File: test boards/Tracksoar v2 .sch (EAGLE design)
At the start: 45 parts, among them IC1 BME280, IC2 74AHC1G125DBV, Y1 16MHZ

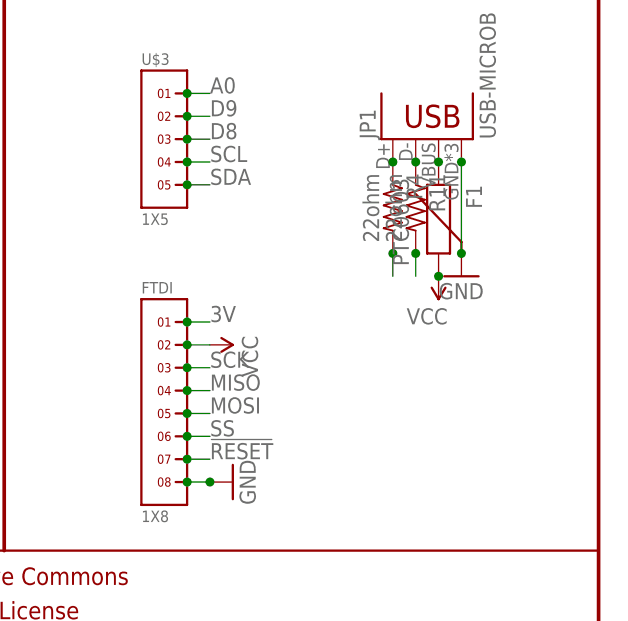
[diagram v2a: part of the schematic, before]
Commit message: Corrected battery connector placement
Moved the battery connector to the bottom side of the board to avoid
conflicts with the USB connector
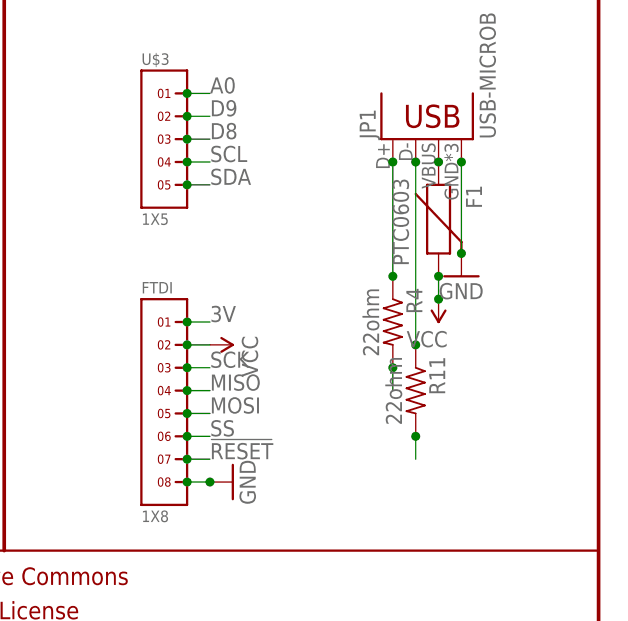
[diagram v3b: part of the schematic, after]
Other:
- moved on the sheet: R11, R4
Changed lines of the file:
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@@
 <instance part="JP1" gate="G$1" x="233.68" y="81.28" rot="R90"/>
 <instance part="J1" gate="G$1" x="38.1" y="177.8" rot="R270"/>
-<instance part="R4" gate="G$1" x="226.06" y="73.66" rot="R270"/>
-<instance part="R11" gate="G$1" x="228.6" y="73.66" rot="R270"/>
+<instance part="R4" gate="G$1" x="226.06" y="60.96" rot="R270"/>
+<instance part="R11" gate="G$1" x="228.6" y="53.34" rot="R270"/>
 <instance part="GND32" gate="1" x="233.68" y="66.04"/>
 <instance part="F1" gate="G$1" x="231.14" y="73.66" rot="R270"/>
-<instance part="SUPPLY15" gate="G$1" x="231.14" y="66.04" rot="R180"/>
+<instance part="SUPPLY15" gate="G$1" x="231.14" y="63.5" rot="R180"/>
 <instance part="SUPPLY16" gate="G$1" x="22.86" y="63.5" rot="R90"/>
 <instance part="C5" gate="G$1" x="12.7" y="58.42" rot="R90"/>
@@
 <pinref part="F1" gate="G$1" pin="2"/>
 <pinref part="SUPPLY15" gate="G$1" pin="VCC"/>
+<wire x1="231.14" y1="63.5" x2="231.14" y2="66.04" width="0.1524" layer="91"/>
 <junction x="231.14" y="66.04"/>
+<junction x="231.14" y="63.5"/>
 </segment>
 <segment>
@@
 <pinref part="JP1" gate="G$1" pin="D-"/>
 <pinref part="R11" gate="G$1" pin="1"/>
+<wire x1="228.6" y1="58.42" x2="228.6" y2="78.74" width="0.1524" layer="91"/>
+<junction x="228.6" y="58.42"/>
 <junction x="228.6" y="78.74"/>
 </segment>
@@
 <pinref part="JP1" gate="G$1" pin="D+"/>
 <pinref part="R4" gate="G$1" pin="1"/>
+<wire x1="226.06" y1="66.04" x2="226.06" y2="78.74" width="0.1524" layer="91"/>
+<junction x="226.06" y="66.04"/>
 <junction x="226.06" y="78.74"/>
 </segment>
@@
 <segment>
 <pinref part="R4" gate="G$1" pin="2"/>
-<wire x1="226.06" y1="68.58" x2="226.06" y2="66.04" width="0.1524" layer="91"/>
-<junction x="226.06" y="68.58"/>
+<wire x1="226.06" y1="55.88" x2="226.06" y2="53.34" width="0.1524" layer="91"/>
+<junction x="226.06" y="55.88"/>
 </segment>
 <segment>
@@
 <segment>
 <pinref part="R11" gate="G$1" pin="2"/>
-<wire x1="228.6" y1="68.58" x2="228.6" y2="66.04" width="0.1524" layer="91"/>
-<junction x="228.6" y="68.58"/>
-</segment>
-<segment>
+<wire x1="228.6" y1="48.26" x2="228.6" y2="45.72" width="0.1524" layer="91"/>
+<junction x="228.6" y="48.26"/>
+</segment>
+<segment>

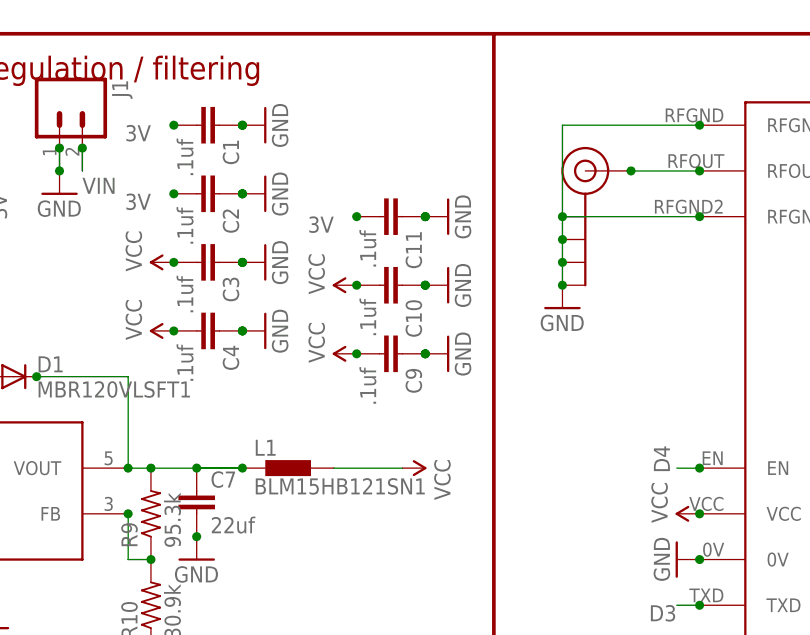
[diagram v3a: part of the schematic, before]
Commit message: Tracksoar V1.3
Created a new test board Tracksoar v1.3 to resolve potential issues
with the boost converter interfering with GPS reception.
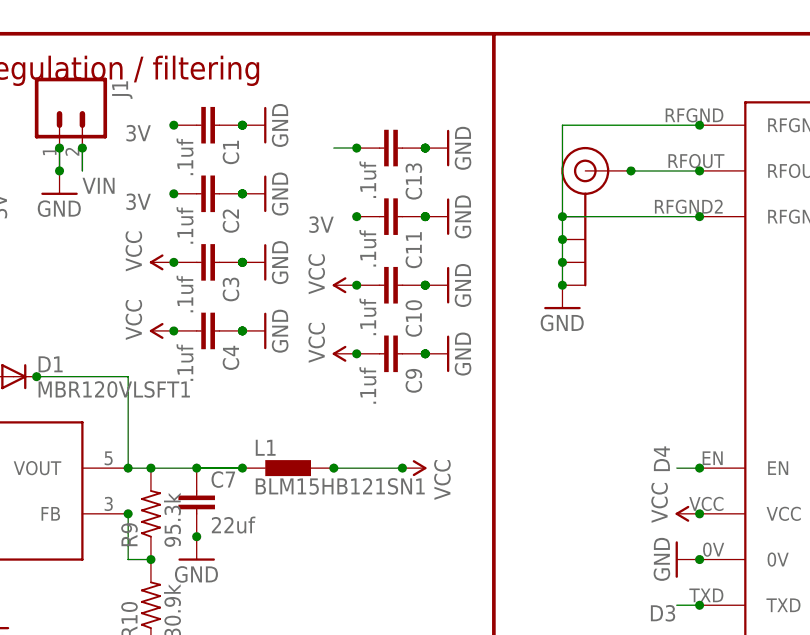
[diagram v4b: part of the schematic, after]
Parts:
- added C13: .1uf, SparkFun-Capacitors:CAP0402-CAP
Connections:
- net GND: now also C13.1
- net VIN: now also C13.2
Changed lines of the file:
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@@
 <grid distance="0.1" unitdist="inch" unit="inch" style="lines" multiple="1" display="no" altdistance="0.01" altunitdist="inch" altunit="inch"/>
 <layers>
-<layer number="1" name="Top" color="4" fill="1" visible="yes" active="no"/>
-<layer number="2" name="Route2" color="1" fill="3" visible="yes" active="no"/>
-<layer number="3" name="Route3" color="4" fill="3" visible="yes" active="no"/>
-<layer number="14" name="Route14" color="1" fill="6" visible="yes" active="no"/>
-<layer number="15" name="Route15" color="4" fill="6" visible="yes" active="no"/>
-<layer number="16" name="Bottom" color="1" fill="1" visible="yes" active="no"/>
-<layer number="17" name="Pads" color="2" fill="1" visible="yes" active="no"/>
-<layer number="18" name="Vias" color="2" fill="1" visible="yes" active="no"/>
-<layer number="19" name="Unrouted" color="6" fill="1" visible="yes" active="no"/>
-<layer number="20" name="Dimension" color="15" fill="1" visible="yes" active="no"/>
-<layer number="21" name="tPlace" color="7" fill="1" visible="yes" active="no"/>
-<layer number="22" name="bPlace" color="7" fill="1" visible="yes" active="no"/>
-<layer number="23" name="tOrigins" color="15" fill="1" visible="yes" active="no"/>
-<layer number="24" name="bOrigins" color="15" fill="1" visible="yes" active="no"/>
-<layer number="25" name="tNames" color="7" fill="1" visible="yes" active="no"/>
-<layer number="26" name="bNames" color="7" fill="1" visible="yes" active="no"/>
-<layer number="27" name="tValues" color="7" fill="1" visible="yes" active="no"/>
-<layer number="28" name="bValues" color="7" fill="1" visible="yes" active="no"/>
+<layer number="1" name="Top" color="4" fill="1" visible="no" active="no"/>
+<layer number="2" name="Route2" color="1" fill="3" visible="no" active="no"/>
+<layer number="3" name="Route3" color="4" fill="3" visible="no" active="no"/>
+<layer number="14" name="Route14" color="1" fill="6" visible="no" active="no"/>
+<layer number="15" name="Route15" color="4" fill="6" visible="no" active="no"/>
+<layer number="16" name="Bottom" color="1" fill="1" visible="no" active="no"/>
+<layer number="17" name="Pads" color="2" fill="1" visible="no" active="no"/>
+<layer number="18" name="Vias" color="2" fill="1" visible="no" active="no"/>
+<layer number="19" name="Unrouted" color="6" fill="1" visible="no" active="no"/>
+<layer number="20" name="Dimension" color="15" fill="1" visible="no" active="no"/>
+<layer number="21" name="tPlace" color="7" fill="1" visible="no" active="no"/>
+<layer number="22" name="bPlace" color="7" fill="1" visible="no" active="no"/>
+<layer number="23" name="tOrigins" color="15" fill="1" visible="no" active="no"/>
+<layer number="24" name="bOrigins" color="15" fill="1" visible="no" active="no"/>
+<layer number="25" name="tNames" color="7" fill="1" visible="no" active="no"/>
+<layer number="26" name="bNames" color="7" fill="1" visible="no" active="no"/>
+<layer number="27" name="tValues" color="7" fill="1" visible="no" active="no"/>
+<layer number="28" name="bValues" color="7" fill="1" visible="no" active="no"/>
 <layer number="29" name="tStop" color="7" fill="3" visible="no" active="no"/>
 <layer number="30" name="bStop" color="7" fill="6" visible="no" active="no"/>
@@
 <layer number="35" name="tGlue" color="7" fill="4" visible="no" active="no"/>
 <layer number="36" name="bGlue" color="7" fill="5" visible="no" active="no"/>
-<layer number="37" name="tTest" color="7" fill="1" visible="yes" active="no"/>
-<layer number="38" name="bTest" color="7" fill="1" visible="yes" active="no"/>
+<layer number="37" name="tTest" color="7" fill="1" visible="no" active="no"/>
+<layer number="38" name="bTest" color="7" fill="1" visible="no" active="no"/>
 <layer number="39" name="tKeepout" color="4" fill="11" visible="no" active="no"/>
 <layer number="40" name="bKeepout" color="1" fill="11" visible="no" active="no"/>
@@
 <layer number="44" name="Drills" color="7" fill="1" visible="no" active="no"/>
 <layer number="45" name="Holes" color="7" fill="1" visible="no" active="no"/>
-<layer number="46" name="Milling" color="3" fill="1" visible="yes" active="no"/>
-<layer number="47" name="Measures" color="7" fill="1" visible="yes" active="no"/>
-<layer number="48" name="Document" color="7" fill="1" visible="yes" active="no"/>
-<layer number="49" name="Reference" color="7" fill="1" visible="yes" active="no"/>
-<layer number="50" name="dxf" color="7" fill="1" visible="yes" active="no"/>
-<layer number="51" name="tDocu" color="7" fill="1" visible="yes" active="no"/>
-<layer number="52" name="bDocu" color="7" fill="1" visible="yes" active="no"/>
-<layer number="53" name="tGND_GNDA" color="7" fill="9" visible="yes" active="no"/>
-<layer number="54" name="bGND_GNDA" color="1" fill="9" visible="yes" active="no"/>
-<layer number="56" name="wert" color="7" fill="1" visible="yes" active="no"/>
-<layer number="57" name="tCAD" color="7" fill="1" visible="yes" active="no"/>
-<layer number="59" name="tCarbon" color="7" fill="1" visible="yes" active="no"/>
-<layer number="60" name="bCarbon" color="7" fill="1" visible="yes" active="no"/>
+<layer number="46" name="Milling" color="3" fill="1" visible="no" active="no"/>
+<layer number="47" name="Measures" color="7" fill="1" visible="no" active="no"/>
+<layer number="48" name="Document" color="7" fill="1" visible="no" active="no"/>
+<layer number="49" name="Reference" color="7" fill="1" visible="no" active="no"/>
+<layer number="50" name="dxf" color="7" fill="1" visible="no" active="no"/>
+<layer number="51" name="tDocu" color="7" fill="1" visible="no" active="no"/>
+<layer number="52" name="bDocu" color="7" fill="1" visible="no" active="no"/>
+<layer number="53" name="tGND_GNDA" color="7" fill="9" visible="no" active="no"/>
+<layer number="54" name="bGND_GNDA" color="1" fill="9" visible="no" active="no"/>
+<layer number="56" name="wert" color="7" fill="1" visible="no" active="no"/>
+<layer number="57" name="tCAD" color="7" fill="1" visible="no" active="no"/>
+<layer number="59" name="tCarbon" color="7" fill="1" visible="no" active="no"/>
+<layer number="60" name="bCarbon" color="7" fill="1" visible="no" active="no"/>
 <layer number="90" name="Modules" color="5" fill="1" visible="yes" active="yes"/>
 <layer number="91" name="Nets" color="2" fill="1" visible="yes" active="yes"/>
@@
 <part name="GND16" library="SparkFun-Aesthetics" deviceset="GND" device=""/>
 <part name="C12" library="SparkFun-Capacitors" deviceset="CAP" device="0402-CAP" value="1uf"/>
+<part name="C13" library="SparkFun-Capacitors" deviceset="CAP" device="0402-CAP" value=".1uf"/>
+<part name="GND19" library="SparkFun-Aesthetics" deviceset="GND" device=""/>
 </parts>
 <sheets>
@@
 <instance part="GND16" gate="1" x="81.28" y="165.1" rot="R90"/>
 <instance part="C12" gate="G$1" x="17.78" y="73.66" rot="R90"/>
+<instance part="C13" gate="G$1" x="73.66" y="172.72" rot="R270"/>
+<instance part="GND19" gate="1" x="81.28" y="172.72" rot="R90"/>
 </instances>
 <busses>
@@
 <label x="7.62" y="73.66" size="1.778" layer="95"/>
 </segment>
+<segment>
+<pinref part="C13" gate="G$1" pin="1"/>
+<pinref part="GND19" gate="1" pin="GND"/>
+<junction x="78.74" y="172.72"/>
+<junction x="78.74" y="172.72"/>
+</segment>
 </net>
 <net name="D3" class="0">
@@
 <pinref part="SUPPLY1" gate="G$1" pin="VCC"/>
 <wire x1="76.2" y1="137.16" x2="68.58" y2="137.16" width="0.1524" layer="91"/>
+<junction x="68.58" y="137.16"/>
+<junction x="76.2" y="137.16"/>
 </segment>
 <segment>
@@
 <label x="116.84" y="43.18" size="1.778" layer="95"/>
 </segment>
-</net>
+<segment>
+<pinref part="C13" gate="G$1" pin="2"/>
+<wire x1="71.12" y1="172.72" x2="68.58" y2="172.72" width="0.1524" layer="91"/>
+<junction x="71.12" y="172.72"/>
+</segment>
+</net>

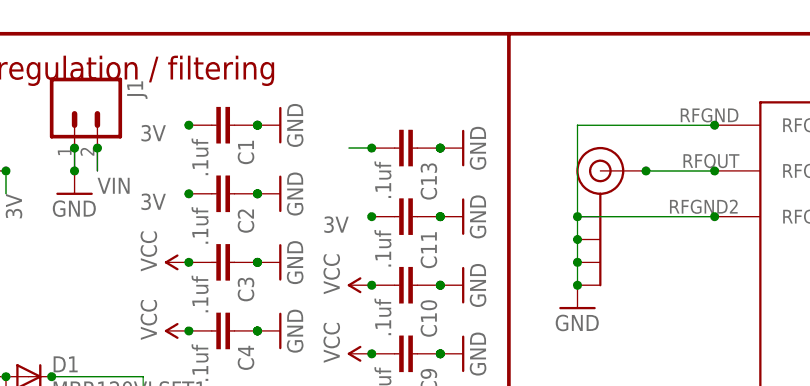
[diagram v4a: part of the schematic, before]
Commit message: v2 BME280 decoupling cap
added decoupling cap to bme280 of v2 board.
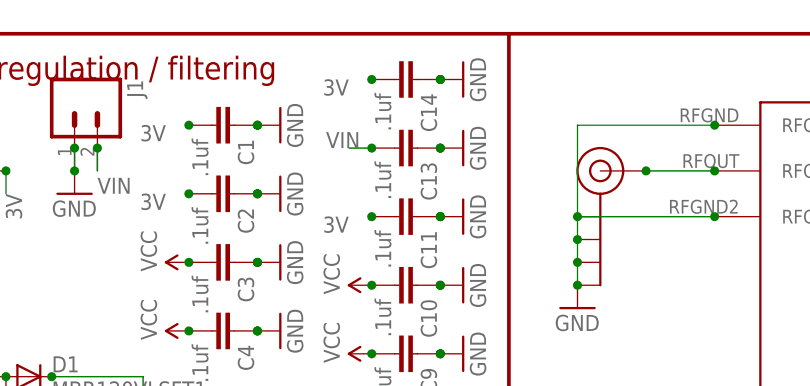
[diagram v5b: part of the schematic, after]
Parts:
- added C14: .1uf, SparkFun-Capacitors:CAP0402-CAP
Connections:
- net 3V: now also C14.2
- net GND: now also C14.1
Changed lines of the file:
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@@
 <part name="C13" library="SparkFun-Capacitors" deviceset="CAP" device="0402-CAP" value=".1uf"/>
 <part name="GND19" library="SparkFun-Aesthetics" deviceset="GND" device=""/>
+<part name="C14" library="SparkFun-Capacitors" deviceset="CAP" device="0402-CAP" value=".1uf"/>
+<part name="GND21" library="SparkFun-Aesthetics" deviceset="GND" device=""/>
 </parts>
 <sheets>
@@
 <instance part="C13" gate="G$1" x="73.66" y="172.72" rot="R270"/>
 <instance part="GND19" gate="1" x="81.28" y="172.72" rot="R90"/>
+<instance part="C14" gate="G$1" x="73.66" y="180.34" rot="R270"/>
+<instance part="GND21" gate="1" x="81.28" y="180.34" rot="R90"/>
 </instances>
 <busses>
@@
 <junction x="78.74" y="172.72"/>
 </segment>
+<segment>
+<pinref part="C14" gate="G$1" pin="1"/>
+<pinref part="GND21" gate="1" pin="GND"/>
+<junction x="78.74" y="180.34"/>
+<junction x="78.74" y="180.34"/>
+</segment>
 </net>
 <net name="D3" class="0">
@@
 <label x="68.58" y="165.1" size="1.778" layer="95" rot="R180"/>
 <junction x="71.12" y="165.1"/>
+</segment>
+<segment>
+<pinref part="C14" gate="G$1" pin="2"/>
+<label x="68.58" y="180.34" size="1.778" layer="95" rot="R180"/>
+<junction x="71.12" y="180.34"/>
 </segment>
 </net>
@@
 <wire x1="71.12" y1="172.72" x2="68.58" y2="172.72" width="0.1524" layer="91"/>
 <junction x="71.12" y="172.72"/>
-</segment>
-</net>
+<label x="66.04" y="172.72" size="1.778" layer="95"/>
+</segment>
+</net>
